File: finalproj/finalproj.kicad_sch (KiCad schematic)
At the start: 46 parts, among them J1 RPI UART, J2 Conn_01x02, J3 Motor_Controller_Connector, J4 DC_Motor_Power_Connector, J5 Stepper_Motor_Controller, J6 Step_Motor_Power_Connector, J7 LIDAR_Connector, J8 Programmer_Conn, U1 STM32F767ZITx, U2 LM1085-12, U3 LM1085-5.0, U4 LM1085-3.3, U5 L298N

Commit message: Full schematic done
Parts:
- removed C? (x3): 0.1u, Capacitor_SMD:C_0805_2012Metric, symbol Device:C_Polarized_US
- removed J1: RPI UART, symbol Connector_Generic:Conn_01x03
- removed J3: Motor_Controller_Connector, symbol finalProj:Motor_Controller_Connector
- added C23: C, symbol Device:C
- added C24, C25: 0.47u, Capacitor_SMD:C_0805_2012Metric, symbol Device:C_Polarized_US
- added C26, C27, C28, C29, C30, C31, C32, C33, C34: 0.1u, Capacitor_SMD:C_0805_2012Metric, symbol Device:C_Polarized_US
- added J1: GPIO_PORT_OUT, Connector_PinHeader_2.54mm:PinHeader_2x08_P2.54mm_Vertical, symbol finalProj:MCU_GPIO_OUT
- added J9: RPI_UART_Conn, symbol finalProj:UART_RPI_CONN
- added POW2: Kinect_Power _Connector, symbol finalProj:Motor_Power_Connector
- added R1: 10k, Resistor_SMD:R_1020_2550Metric_Pad1.33x5.20mm_HandSolder, symbol Device:R
- J8: footprint (none) -> Connector_PinHeader_2.54mm:PinHeader_1x06_P2.54mm_Vertical
- POW1: renamed from J2; value Conn_01x02 -> POWER_IN
- POW3: renamed from J6; footprint (none) -> TerminalBlock_Phoenix:TerminalBlock_Phoenix_PT-1,5-2-3.5-H_1x02_P3.50mm_Horizontal
- POW4: renamed from J4; footprint (none) -> TerminalBlock_Phoenix:TerminalBlock_Phoenix_PT-1,5-2-3.5-H_1x02_P3.50mm_Horizontal
- SW1: renamed from SW?; value SW_Push -> RESET_SW; footprint (none) -> Button_Switch_THT:SW_PUSH_6mm
- U5: footprint Package_TO_SOT_THT:TO-220-15_P2.54x2.54mm_StaggerOdd_Lead4.58mm_Vertical -> Package_TO_SOT_THT:TO-220-15_P2.54x2.54mm_StaggerOdd_Lead5.84mm_TabDown
- gave numbers to parts that had none: 1
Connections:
- net +12V: now also U2.2 (VO), C26.1, C29.1, C30.1, POW2.1 (VIN); no longer U4.2 (VO)
- net +3.3V: now also U4.2 (VO), C28.1, C33.1, C34.1; no longer U3.2 (VO)
- net +5V: now also U3.2 (VO), C27.1, C31.1, C32.1, J9.1 (VIN); no longer U2.2 (VO)
- net GND: now also C35.2, SW1.2, C23.2, C24.2, C25.2, C26.2, C27.2, C28.2, C29.2, C30.2, C31.2, C32.2, C33.2, C34.2, J9.4 (GND), POW2.2 (GND), R1.2
- net MotorAPWM: now also U1.42 (PA6), J1.7 (Pin_7); no longer U1.106 (VCAP_2)
- net MotorBPWM: now also U1.81 (PD12); no longer U1.65 (PE12)
- net RPI_UART_RX: now also J9.3 (RX)
- net RPI_UART_TX: now also J9.2 (TX)
- net STEP_DIR: now also U1.59 (PE8); no longer U1.77 (PD8)
- net STEP_PWM: now also U1.60 (PE9); no longer U1.78 (PD9)
- net at POW1.2 (Pin_2), U2.3 (VI), U3.3 (VI): now also C35.1, C24.1; no longer U4.3 (VI)
- net at U1.23 (PH0): no longer J8.2 (SWCLK)
- net SWDIO: now reaches J8.4 (SWDIO)
- net SWDIO: now also U1.105 (PA13), J1.14 (Pin_14)
- net at J8.5 (NRST): now also SW1.1, U1.25 (NRST), C23.1
- net at U1.100 (PA8): now also J1.9 (Pin_9)
- net at U1.101 (PA9): now also J1.10 (Pin_10)
- net at U1.102 (PA10): now also J1.11 (Pin_11)
- net at U1.103 (PA11): now also J1.12 (Pin_12)
- net at U1.104 (PA12): now also J1.13 (Pin_13)
- net SWCLK: now reaches U1.109 (PA14)
- net SWCLK: now also J8.2 (SWCLK), J1.15 (Pin_15)
- net at U1.110 (PA15): now also J1.16 (Pin_16)
- net at U1.138 (BOOT0): now also R1.1
- net at U1.34 (PA0): now also J1.1 (Pin_1)
- net at U1.35 (PA1): now also J1.2 (Pin_2)
- net at U1.36 (PA2): now also J1.3 (Pin_3)
- net at U1.37 (PA3): now also J1.4 (Pin_4)
- net at U1.40 (PA4): now also J1.5 (Pin_5)
- net at U1.41 (PA5): now also J1.6 (Pin_6)
- net at U1.43 (PA7): now also J1.8 (Pin_8)
- new net: C25.1, U4.3 (VI)
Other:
- note added: "DC Motor"
- note added: "RPI"
- note added: "StepperMotor"
- note removed: "Motor"
- moved on the sheet: C1, C2, C35, D1, D2, D3, D4, J8, POW1, SW1, U5, U8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

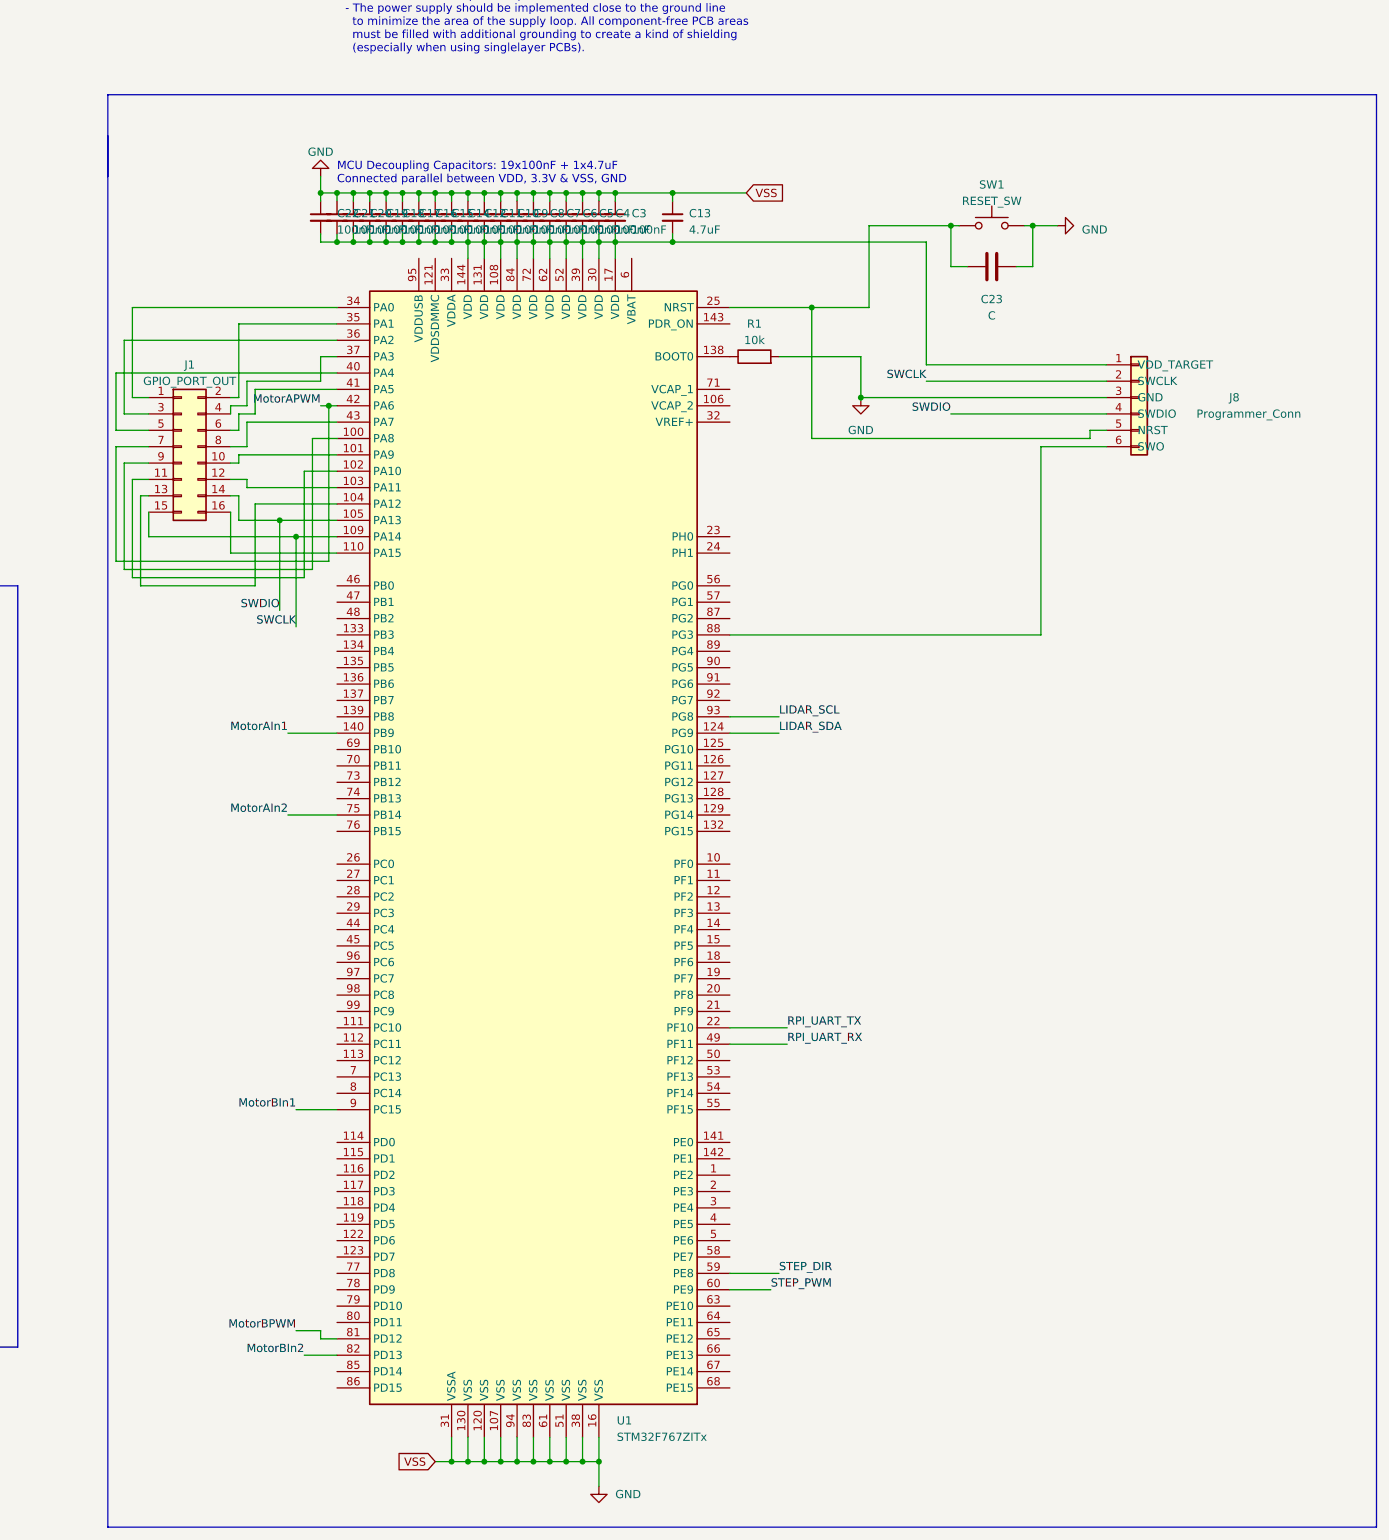
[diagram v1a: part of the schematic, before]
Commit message: changed mcu to sockets
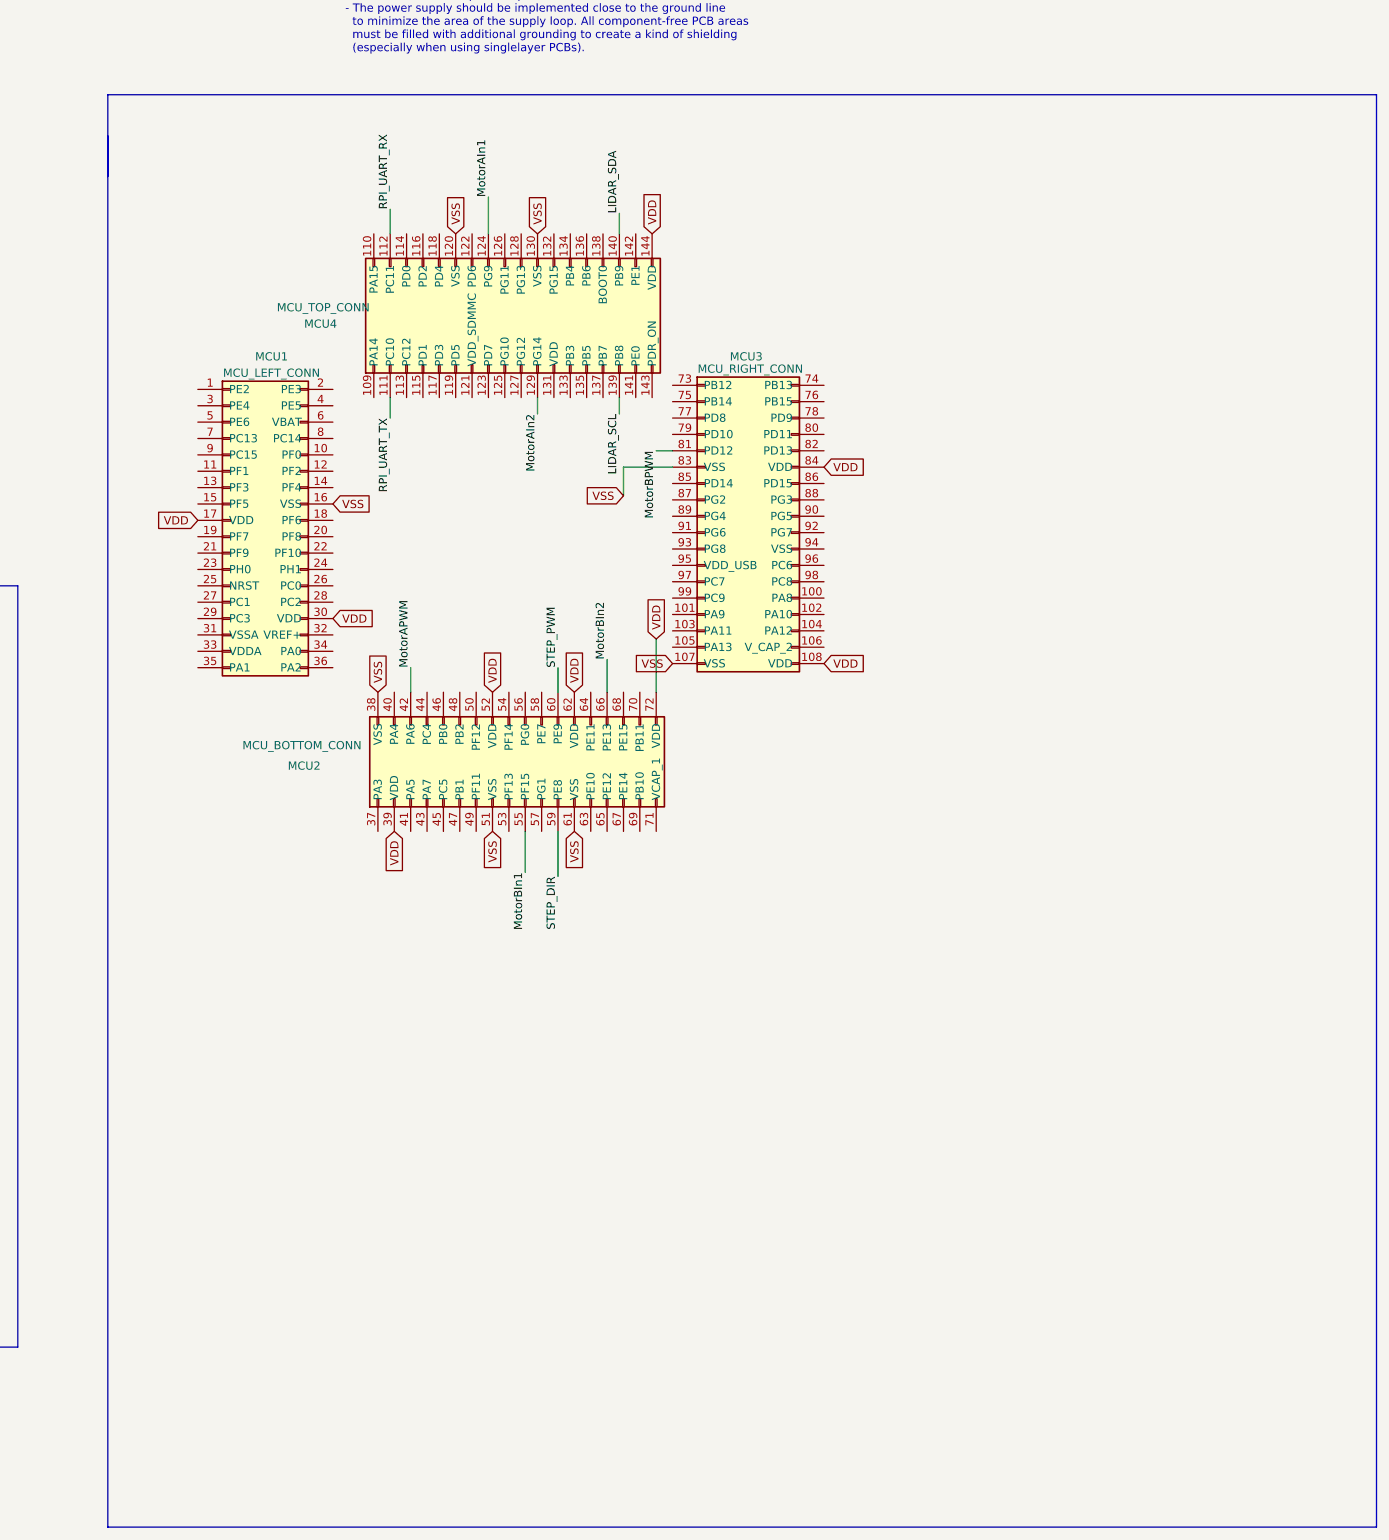
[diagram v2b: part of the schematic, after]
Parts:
- removed C10, C11, C12, C14, C15, C16, C17, C18, C19, C20, C21, C22, C3, C4, C5, C6, C7, C8, C9: 100nF, symbol Device:C_Small
- removed C13: 4.7uF, symbol Device:C_Small
- removed C23: C, symbol Device:C
- removed J1: GPIO_PORT_OUT, Connector_PinHeader_2.54mm:PinHeader_2x08_P2.54mm_Vertical, symbol finalProj:MCU_GPIO_OUT
- removed J8: Programmer_Conn, Connector_PinHeader_2.54mm:PinHeader_1x06_P2.54mm_Vertical, symbol finalProj:Programmer_Conn
- removed R1: 10k, Resistor_SMD:R_1020_2550Metric_Pad1.33x5.20mm_HandSolder, symbol Device:R
- removed SW1: RESET_SW, Button_Switch_THT:SW_PUSH_6mm, symbol Switch:SW_Push
- removed U1: STM32F767ZITx, Package_QFP:LQFP-144_20x20mm_P0.5mm, symbol MCU_ST_STM32F7:STM32F767ZITx
- added MCU1: MCU_LEFT_CONN, Connector_PinSocket_2.54mm:PinSocket_2x18_P2.54mm_Vertical, symbol Connector_Generic:Conn_02x18_Odd_Even
- added MCU2: MCU_BOTTOM_CONN, Connector_PinSocket_2.54mm:PinSocket_2x18_P2.54mm_Vertical, symbol Connector_Generic:Conn_02x18_Odd_Even
- added MCU3: MCU_RIGHT_CONN, Connector_PinSocket_2.54mm:PinSocket_2x18_P2.54mm_Vertical, symbol Connector_Generic:Conn_02x18_Odd_Even
- added MCU4: MCU_TOP_CONN, Connector_PinSocket_2.54mm:PinSocket_2x18_P2.54mm_Vertical, symbol Connector_Generic:Conn_02x18_Odd_Even
- J5: footprint (none) -> TerminalBlock_Phoenix:TerminalBlock_Phoenix_PT-1,5-9-3.5-H_1x09_P3.50mm_Horizontal
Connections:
- net LIDAR_SCL: now also MCU4.139 (PB8)
- net LIDAR_SDA: now also MCU4.140 (PB9)
- net MotorAIn1: now also MCU4.124 (PG9)
- net MotorAIn2: now also MCU4.129 (PG14)
- net MotorAPWM: now also MCU2.42 (PA6)
- net MotorBIn1: now also MCU2.55 (PF15)
- net MotorBIn2: now also MCU2.66 (PE13)
- net MotorBPWM: now also MCU3.81 (PD12)
- net RPI_UART_RX: now also MCU4.112 (PC11)
- net RPI_UART_TX: now also MCU4.111 (PC10)
- net STEP_DIR: now also MCU2.59 (PE8)
- net STEP_PWM: now also MCU2.60 (PE9)
- new net VDD: MCU1.17 (VDD), MCU1.30 (VDD), MCU2.39 (VDD), MCU2.52 (VDD), MCU2.62 (VDD), MCU2.72 (VDD), MCU3.108 (VDD), MCU3.84 (VDD), MCU4.144 (VDD)
- new net VSS: MCU1.16 (VSS), MCU2.38 (VSS), MCU2.51 (VSS), MCU2.61 (VSS), MCU3.107 (VSS), MCU3.83 (VSS), MCU4.120 (VSS), MCU4.130 (VSS)
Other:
- note removed: "MCU Decoupling Capacitors: 19x100nF + 1x4.7uF Connected parallel between VDD, 3.3V & VSS, GND"
